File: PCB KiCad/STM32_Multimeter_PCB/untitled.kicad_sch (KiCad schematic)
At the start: 25 parts, among them J6 Barrel_Jack, J8 Barrel_Jack, J9 Barrel_Jack, Q1 NMOS, Q2 NMOS, Q3 NMOS, Q4 NMOS, Q5 NMOS

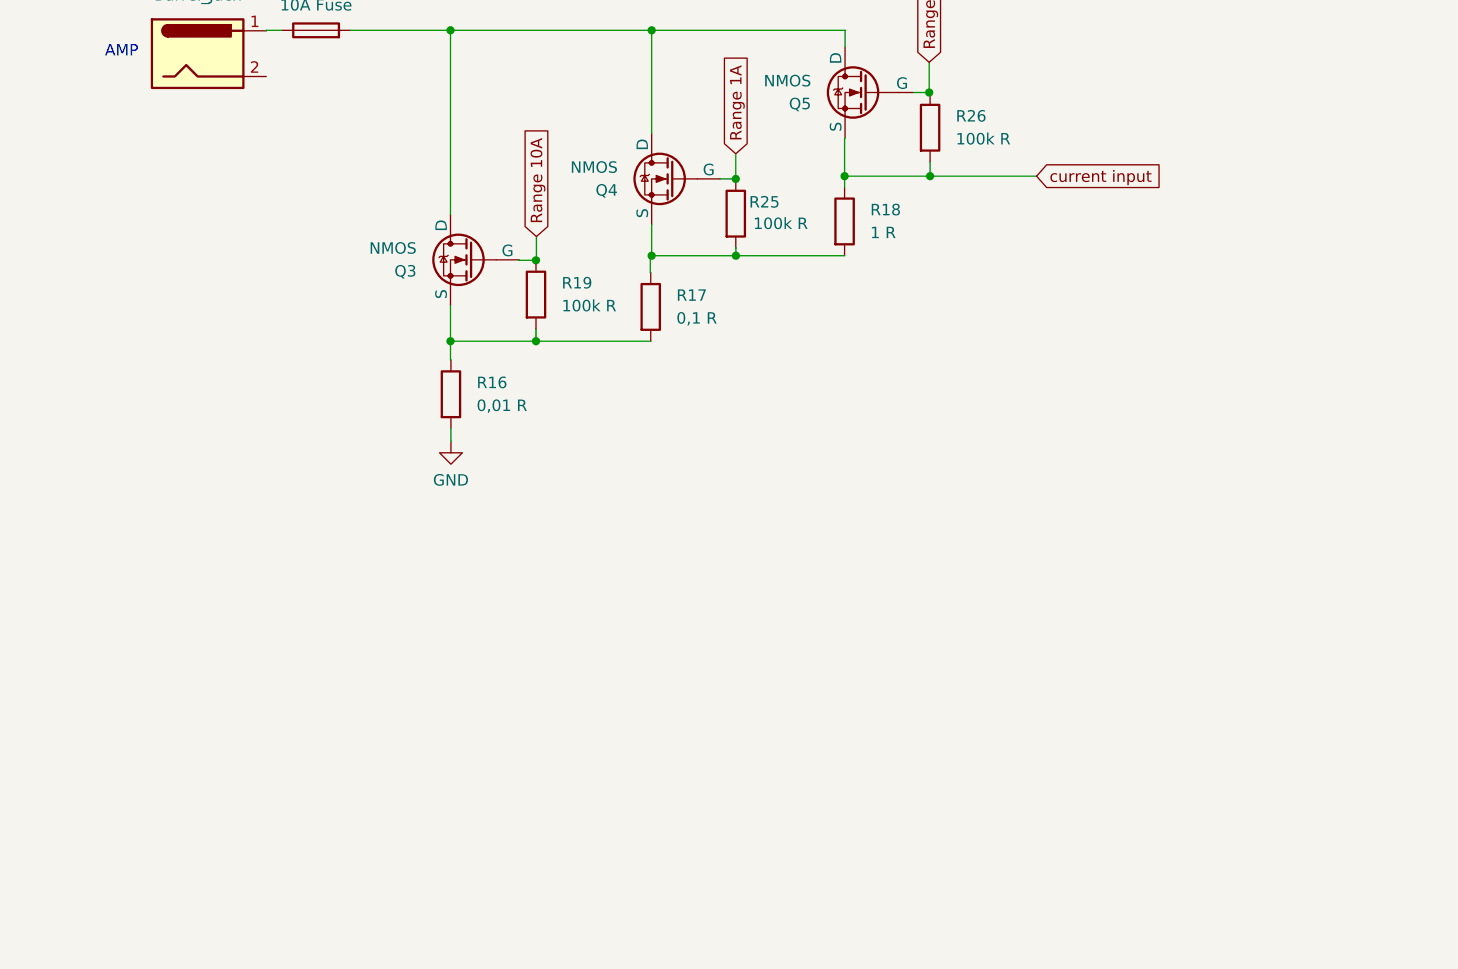
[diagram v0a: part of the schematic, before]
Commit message: Added resistance measurement circuitry
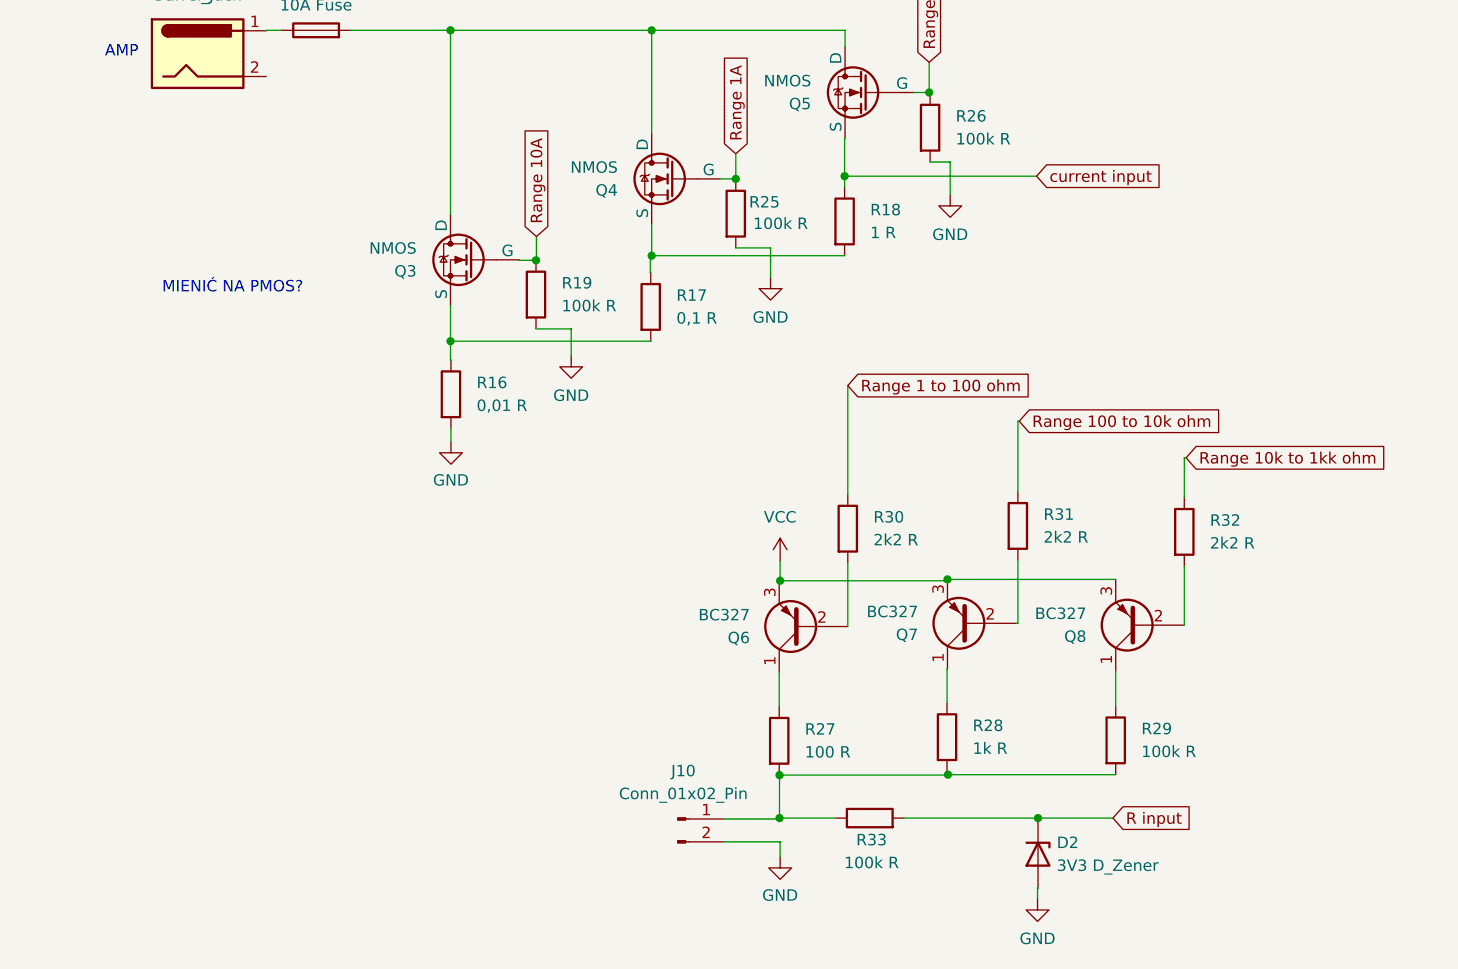
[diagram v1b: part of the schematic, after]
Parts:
- added D2: 3V3 D_Zener, symbol Device:D_Zener
- added J10: Conn_01x02_Pin, symbol Connector:Conn_01x02_Pin
- added Q6, Q7, Q8: BC327, Package_TO_SOT_THT:TO-92_Inline, symbol Transistor_BJT:BC327
- added R27: 100 R, symbol Device:R
- added R28: 1k R, symbol Device:R
- added R29, R33: 100k R, symbol Device:R
- added R30, R31, R32: 2k2 R, symbol Device:R
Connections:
- net GND: now also R19.2, R25.2, R26.2, D2.2 (A), J10.2 (Pin_2)
- net current input: no longer R26.2
- net at Q4.3 (S), R17.1, R18.2: no longer R25.2
- net at Q3.3 (S), R16.1, R17.2: no longer R19.2
- new net: J10.1 (Pin_1), R27.2, R28.2, R29.2, R33.1
- new net: Q7.1 (C), R28.1
- new net: Q7.2 (B), R31.2
- new net: Q6.1 (C), R27.1
- new net: Q6.2 (B), R30.2
- new net: Q8.1 (C), R29.1
- new net: Q8.2 (B), R32.2
- new net R input: D2.1 (K), R33.2
- new net Range 1 to 100 ohm: R30.1
- new net Range 100 to 10k ohm: R31.1
- new net Range 10k to 1kk ohm: R32.1
- new net VCC: Q6.3 (E), Q7.3 (E), Q8.3 (E)
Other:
- note added: "MIENIĆ NA PMOS?"

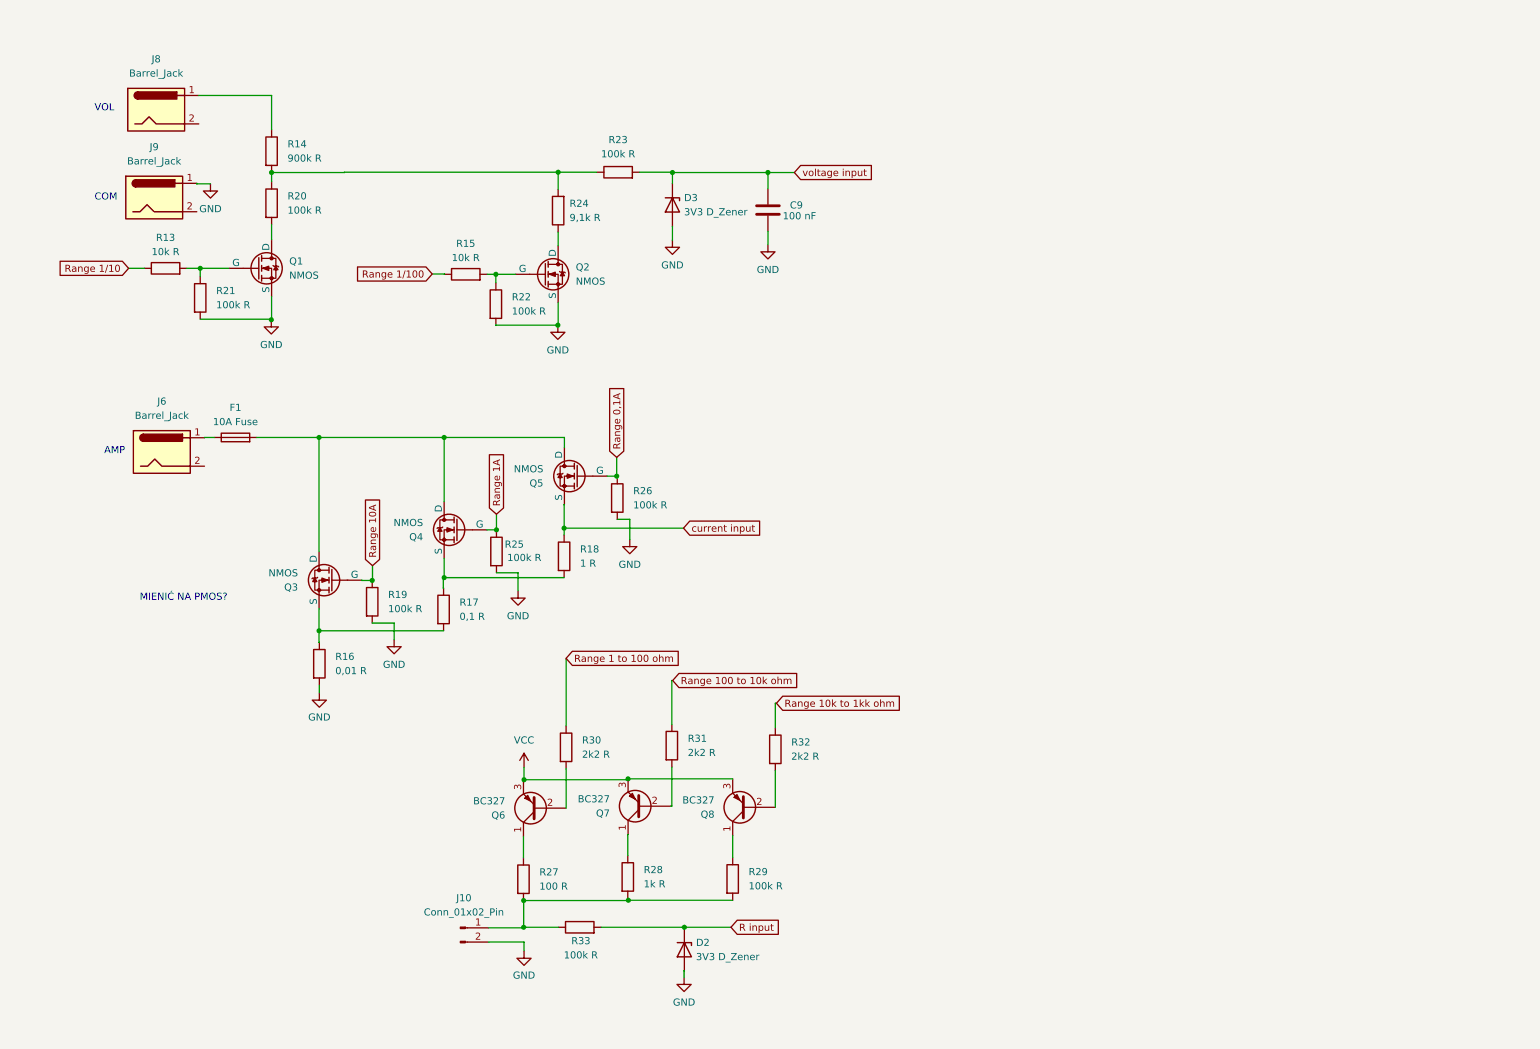
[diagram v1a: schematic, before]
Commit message: Changed RF filter
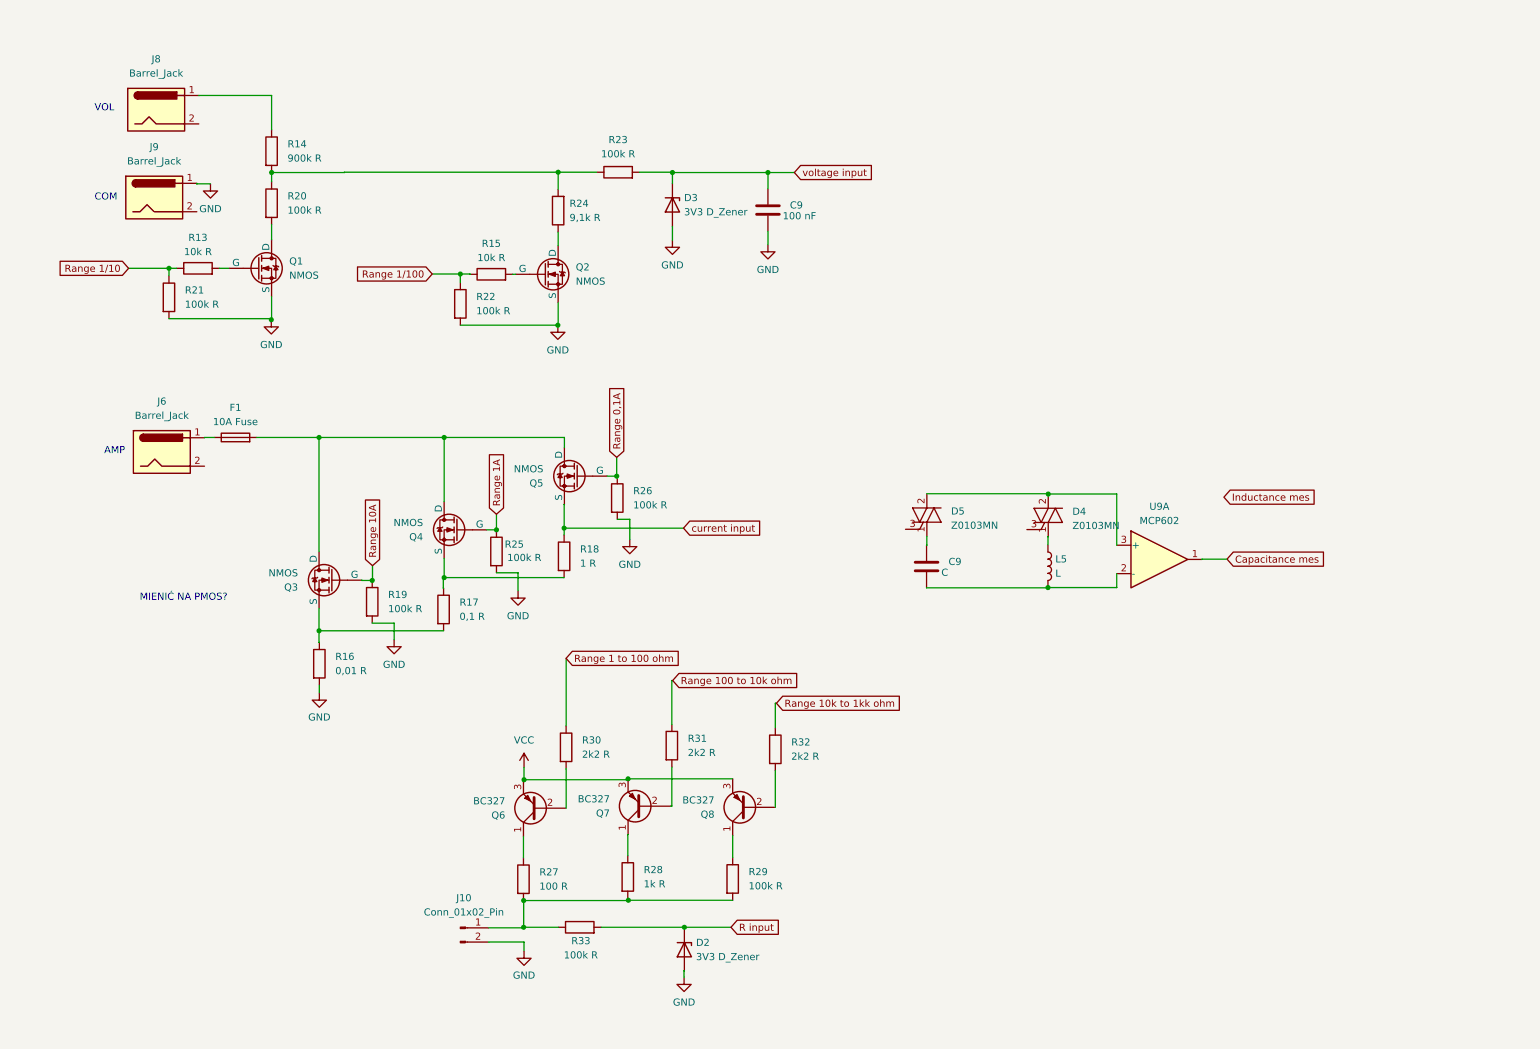
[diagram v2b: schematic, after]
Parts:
- added C9: C, symbol Device:C
- added D4, D5: Z0103MN, Package_TO_SOT_SMD:SOT-223, symbol Triac_Thyristor:Z0103MN
- added L5: L, symbol Device:L
- added U9: MCP602, symbol Amplifier_Operational:MCP602
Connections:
- net Range 1/10: now also R21.1
- net Range 1/100: now also R22.1
- net at Q1.2 (G), R13.2: no longer R21.1
- net at Q2.2 (G), R15.2: no longer R22.1
- new net: C9.1, D5.1 (A1)
- new net: D4.2 (A2), D4.4 (A4), D5.2 (A2), D5.4 (A4), U9.3 (+)
- new net: D4.1 (A1), L5.1
- new net: C9.2, L5.2, U9.2 (-)
- new net Capacitance mes: U9.1
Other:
- moved on the sheet: R13, R15, R21, R22

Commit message: Added LC osicilator for inductance and capacitance measurment
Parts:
- added D6: 1N4148W, Diode_SMD:D_SOD-123, symbol Diode:1N4148W
- added J7: Conn_01x02_Pin, symbol Connector:Conn_01x02_Pin
- added Q9: BC327, Package_TO_SOT_THT:TO-92_Inline, symbol Transistor_BJT:BC327
- added R34, R35, R37: 2k2 R, symbol Device:R
- added R36: 220 R, symbol Device:R
- C9: value C -> 1uF
- L5: value L -> 10uH
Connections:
- net GND: now also C9.2, L5.2, U9.2 (-), J7.2 (Pin_2)
- net VCC: now also Q9.3 (E)
- net at D4.2 (A2), D4.4 (A4), D5.2 (A2)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: now also D6.1 (K), J7.1 (Pin_1)
- net at D5.3 (G): now also R34.1
- net at D4.3 (G): now also R35.1
- net Capacitance mes renamed CL input
- new net: Q9.1 (C), R36.2
- new net: Q9.2 (B), R37.1
- new net: D6.2 (A), R36.1
- new net C on: R34.2
- new net L on: R35.2
- new net charge LC: R37.2
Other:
- note removed: "MIENIĆ NA PMOS?"
- moved on the sheet: C9, D4, D5, L5, U9A

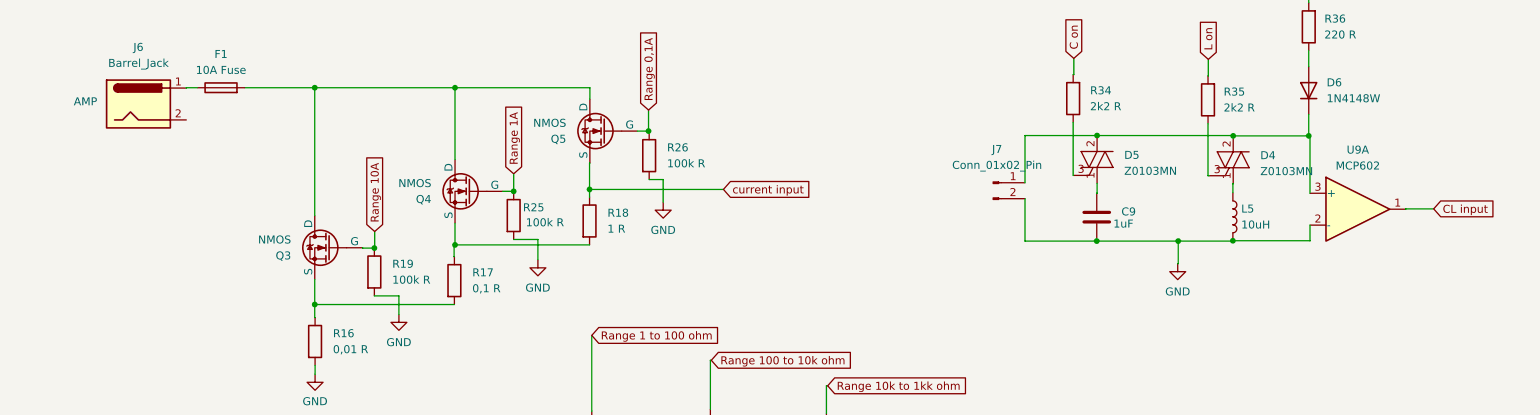
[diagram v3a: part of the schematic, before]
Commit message: Added 9V SMPS, swiched 3,3V SMPS to linnear regulator
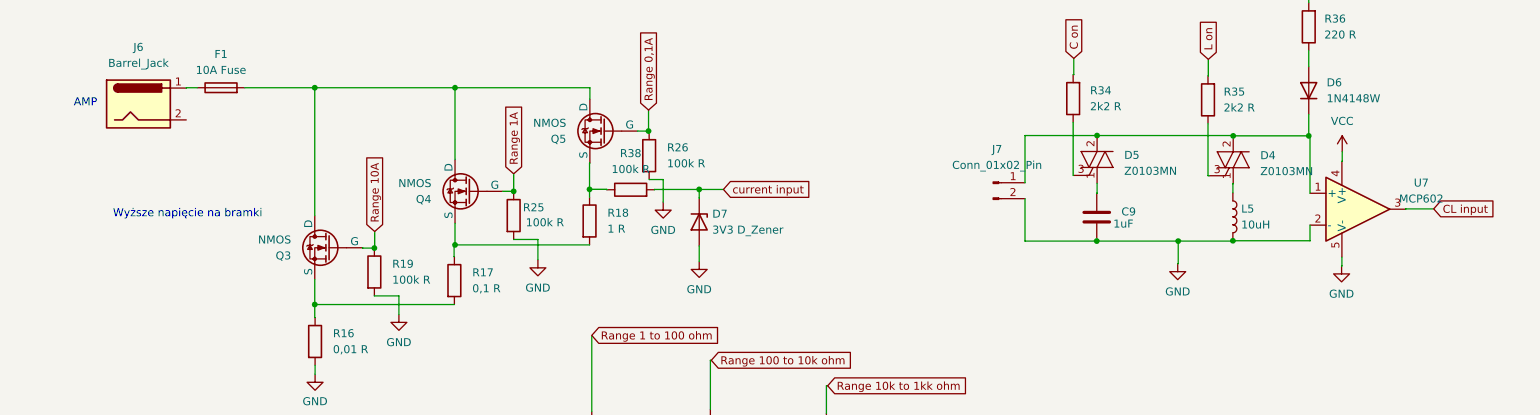
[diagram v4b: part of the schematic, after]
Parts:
- removed U9: MCP602, symbol Amplifier_Operational:MCP602
- added D7: 3V3 D_Zener, Resistor_SMD:R_1206_3216Metric_Pad1.30x1.75mm_HandSolder, symbol Device:D_Zener
- added R38: 100k R, Resistor_SMD:R_0805_2012Metric, symbol Device:R
- added U7: MCP602, symbol Simulation_SPICE:OPAMP
- C9: footprint (none) -> Capacitor_SMD:C_0805_2012Metric
- D2, D3: footprint (none) -> Resistor_SMD:R_1206_3216Metric_Pad1.30x1.75mm_HandSolder
- J10, J7: footprint (none) -> Connector_PinHeader_2.54mm:PinHeader_1x02_P2.54mm_Vertical
- Q6, Q7, Q8, Q9: footprint Package_TO_SOT_THT:TO-92_Inline -> Package_TO_SOT_SMD:SOT-23-3
- R13, R14, R15, R19, R20, R21, R22, R23, R24, R25, R26, R27, R28, R29, R30, R31, R32, R33, R34, R35, R36, R37: footprint (none) -> Resistor_SMD:R_0805_2012Metric
- R16, R17, R18: footprint (none) -> Resistor_SMD:R_MELF_MMB-0207
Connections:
- net CL input: now also U7.3
- net GND: now also D7.2 (A), U7.2 (-), U7.5 (V-)
- net VCC: now also U7.4 (V+)
- net current input: now also D7.1 (K), R38.2; no longer Q5.3 (S), R18.1
- net at D4.2 (A2), D4.4 (A4), D5.2 (A2)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: now also U7.1 (+)
- new net: Q5.3 (S), R18.1, R38.1
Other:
- note added: "Wyższe napięcie na bramki"
